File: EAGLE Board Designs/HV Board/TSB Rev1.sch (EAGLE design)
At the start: 148 parts, among them J1 CONNECTOR-4_MOLEX_MICROFIT_PT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, J2 CONNECTOR-3_MOLEX_MICROFIT_PT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, J3 CONNECTOR-8_MF_T_V_, J4 CONNECTOR-3_MOLEX_MICROFIT_PT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, J5 CONNECTOR-4__, K4 RELAY_SPST_NC_POLARIZED_3550_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, K5 RELAY_SPST_NO_3550_12, Q2 TRANSISTOR_N_MOS__PMV15ENEA, U1 LTC6994_1, U10 DCM4623TD2J13D0T70, U11 RELAY_SOLIDSTATE_NC, U15 LOGICGATE_INVERTER_DCKR, U16 LTC3639, U17 VOLTAGE_REGULATOR_ADJ_LR8_SOT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, U18 ISO224B_AIRGAP, U19 ISO224B_AIRGAP, U2 VOLTAGE_REGULATOR_SOT223_5V

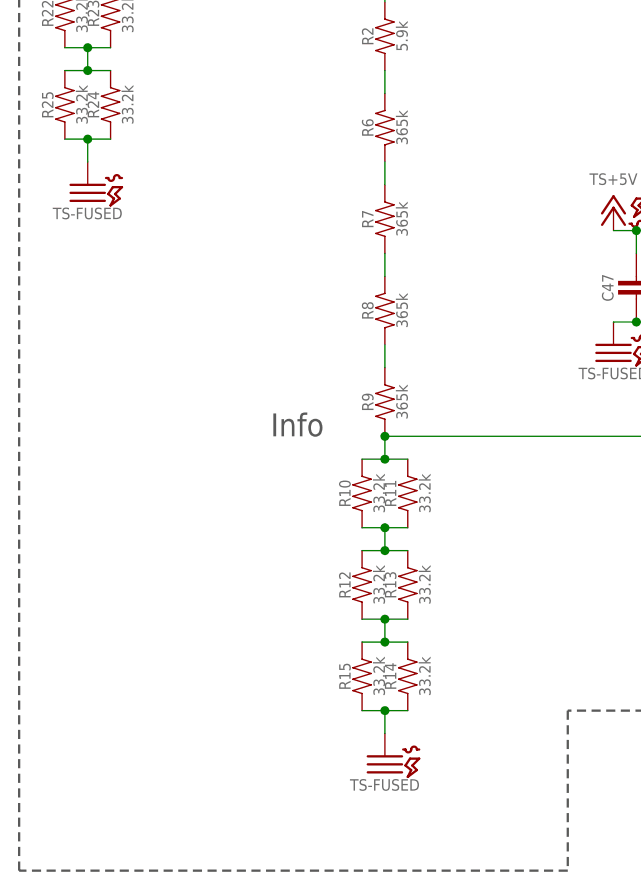
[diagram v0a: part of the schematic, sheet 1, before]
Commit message: fized more erc errors
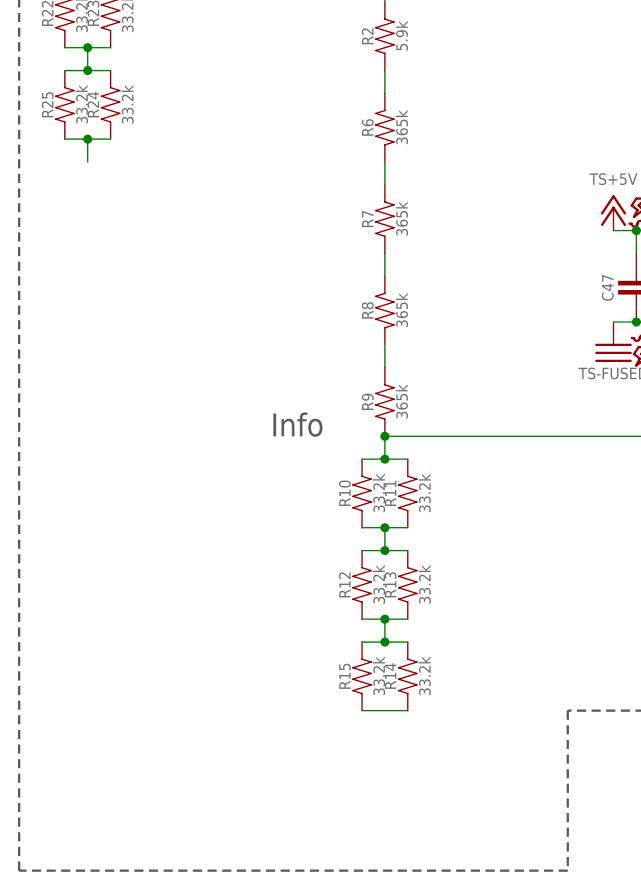
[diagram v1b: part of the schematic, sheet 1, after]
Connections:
- new net N$1: R24.1, R25.1
- new net N$36: R14.1, R15.1
- net TS-FUSED: no longer R14.1, R15.1, R24.1, R25.1
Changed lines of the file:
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@@
 <part name="J4" library="HyTechDevices" deviceset="CONNECTOR-3_?" device="MOLEX_MICROFIT_PTH_VERTICAL_7_DUAL_SPACED2"/>
 <part name="F2" library="HyTechDevices" deviceset="FUSE_?_*" device="0885" technology="1.25"/>
-<part name="U$4" library="HyTechSupplies" deviceset="TS-FUSED" device=""/>
-<part name="U$16" library="HyTechSupplies" deviceset="TS-FUSED" device=""/>
 <part name="U$17" library="HyTechSupplies" deviceset="TS-FUSED" device=""/>
 <part name="U$22" library="HyTechSupplies" deviceset="TS-FUSED" device=""/>
@@
 <attribute name="NAME" x="255.524" y="179.07" size="1.27" layer="96" rot="MR270" align="bottom-center"/>
 </instance>
-<instance part="U$4" gate="G$1" x="17.78" y="93.98" smashed="yes">
-<attribute name="VALUE" x="17.78" y="91.44" size="1.27" layer="96" align="top-center"/>
-</instance>
-<instance part="U$16" gate="G$1" x="50.8" y="30.48" smashed="yes">
-<attribute name="VALUE" x="50.8" y="27.94" size="1.27" layer="96" align="top-center"/>
-</instance>
 <instance part="U$17" gate="G$1" x="96.52" y="50.8" smashed="yes">
 <attribute name="VALUE" x="96.52" y="48.26" size="1.27" layer="96" align="top-center"/>
@@
 </net>
 <net name="TS-FUSED" class="0">
-<segment>
-<pinref part="R25" gate="G$1" pin="1"/>
-<pinref part="R24" gate="G$1" pin="1"/>
-<wire x1="15.24" y1="99.06" x2="17.78" y2="99.06" width="0.1524" layer="91"/>
-<wire x1="17.78" y1="99.06" x2="20.32" y2="99.06" width="0.1524" layer="91"/>
-<wire x1="17.78" y1="99.06" x2="17.78" y2="96.52" width="0.1524" layer="91"/>
-<junction x="17.78" y="99.06"/>
-<pinref part="U$4" gate="G$1" pin="TS-UNFUSED"/>
-</segment>
-<segment>
-<pinref part="R15" gate="G$1" pin="1"/>
-<pinref part="R14" gate="G$1" pin="1"/>
-<wire x1="48.26" y1="35.56" x2="50.8" y2="35.56" width="0.1524" layer="91"/>
-<wire x1="50.8" y1="35.56" x2="53.34" y2="35.56" width="0.1524" layer="91"/>
-<wire x1="50.8" y1="35.56" x2="50.8" y2="33.02" width="0.1524" layer="91"/>
-<junction x="50.8" y="35.56"/>
-<pinref part="U$16" gate="G$1" pin="TS-UNFUSED"/>
-</segment>
 <segment>
 <pinref part="C49" gate="G$1" pin="2"/>
@@
 </segment>
 </net>
+<net name="N$1" class="0">
+<segment>
+<pinref part="R25" gate="G$1" pin="1"/>
+<pinref part="R24" gate="G$1" pin="1"/>
+<wire x1="15.24" y1="99.06" x2="17.78" y2="99.06" width="0.1524" layer="91"/>
+<wire x1="17.78" y1="99.06" x2="20.32" y2="99.06" width="0.1524" layer="91"/>
+<wire x1="17.78" y1="99.06" x2="17.78" y2="96.52" width="0.1524" layer="91"/>
+<junction x="17.78" y="99.06"/>
+</segment>
+</net>
+<net name="N$36" class="0">
+<segment>
+<pinref part="R15" gate="G$1" pin="1"/>
+<pinref part="R14" gate="G$1" pin="1"/>
+<wire x1="48.26" y1="35.56" x2="53.34" y2="35.56" width="0.1524" layer="91"/>
+</segment>
+</net>

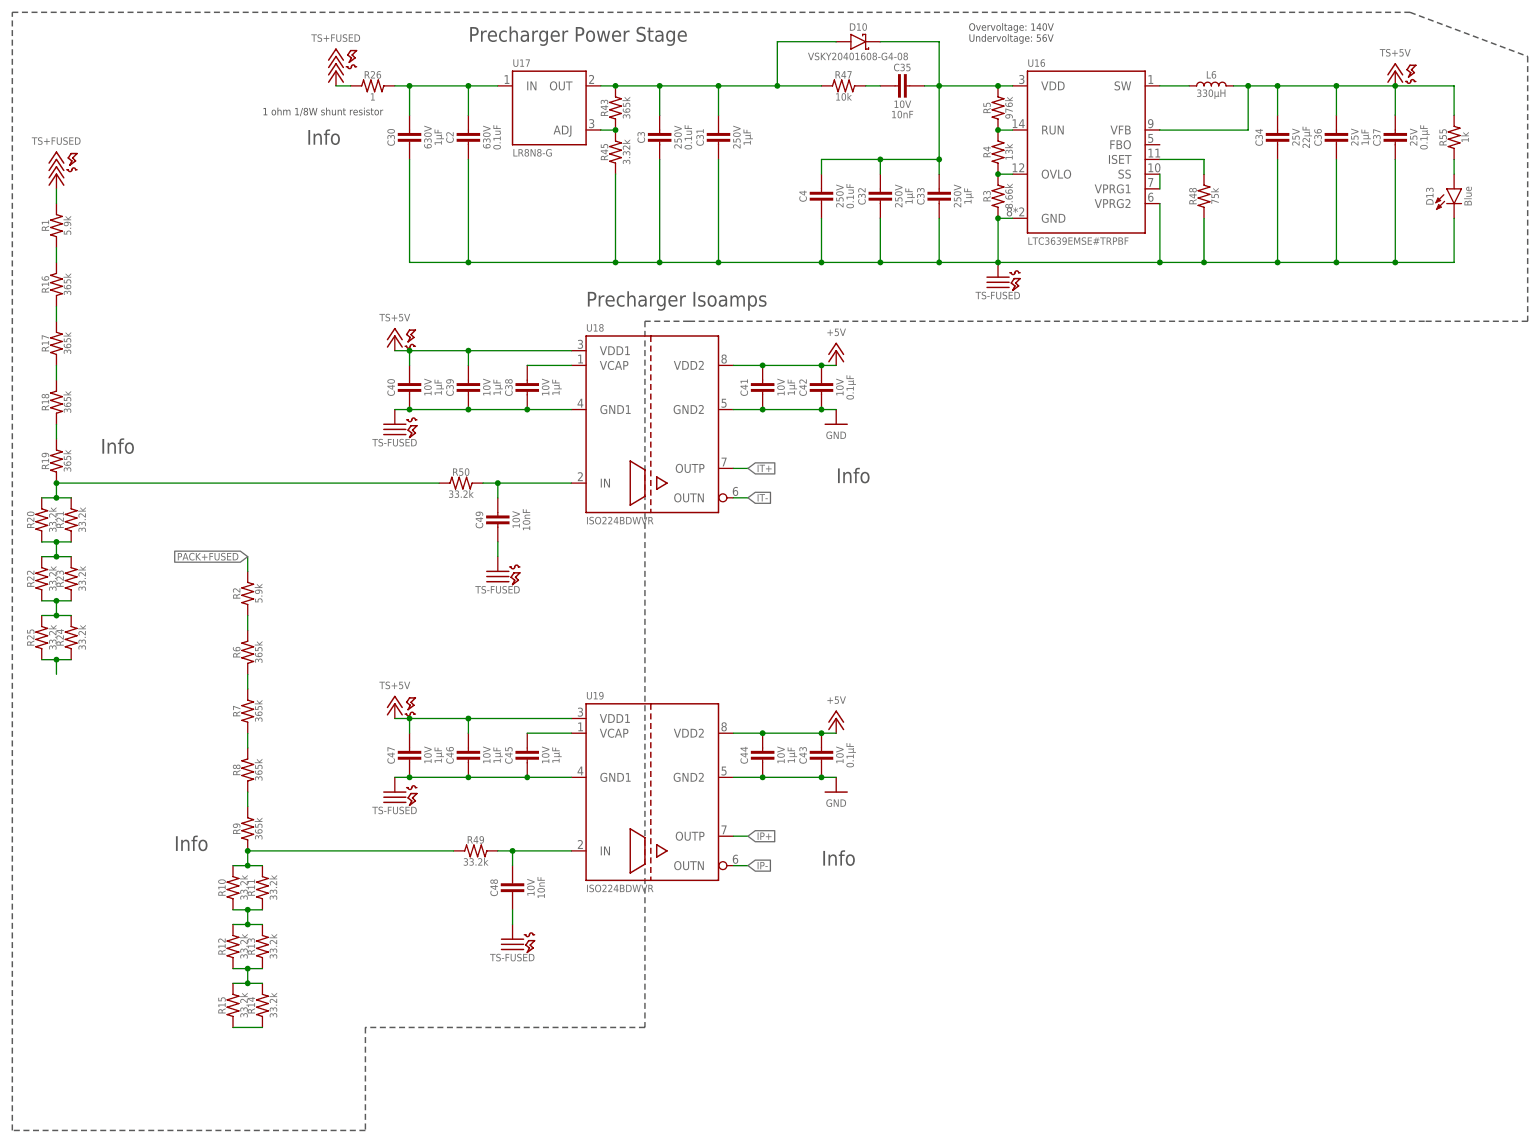
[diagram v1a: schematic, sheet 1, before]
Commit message: Fixed all erc errors
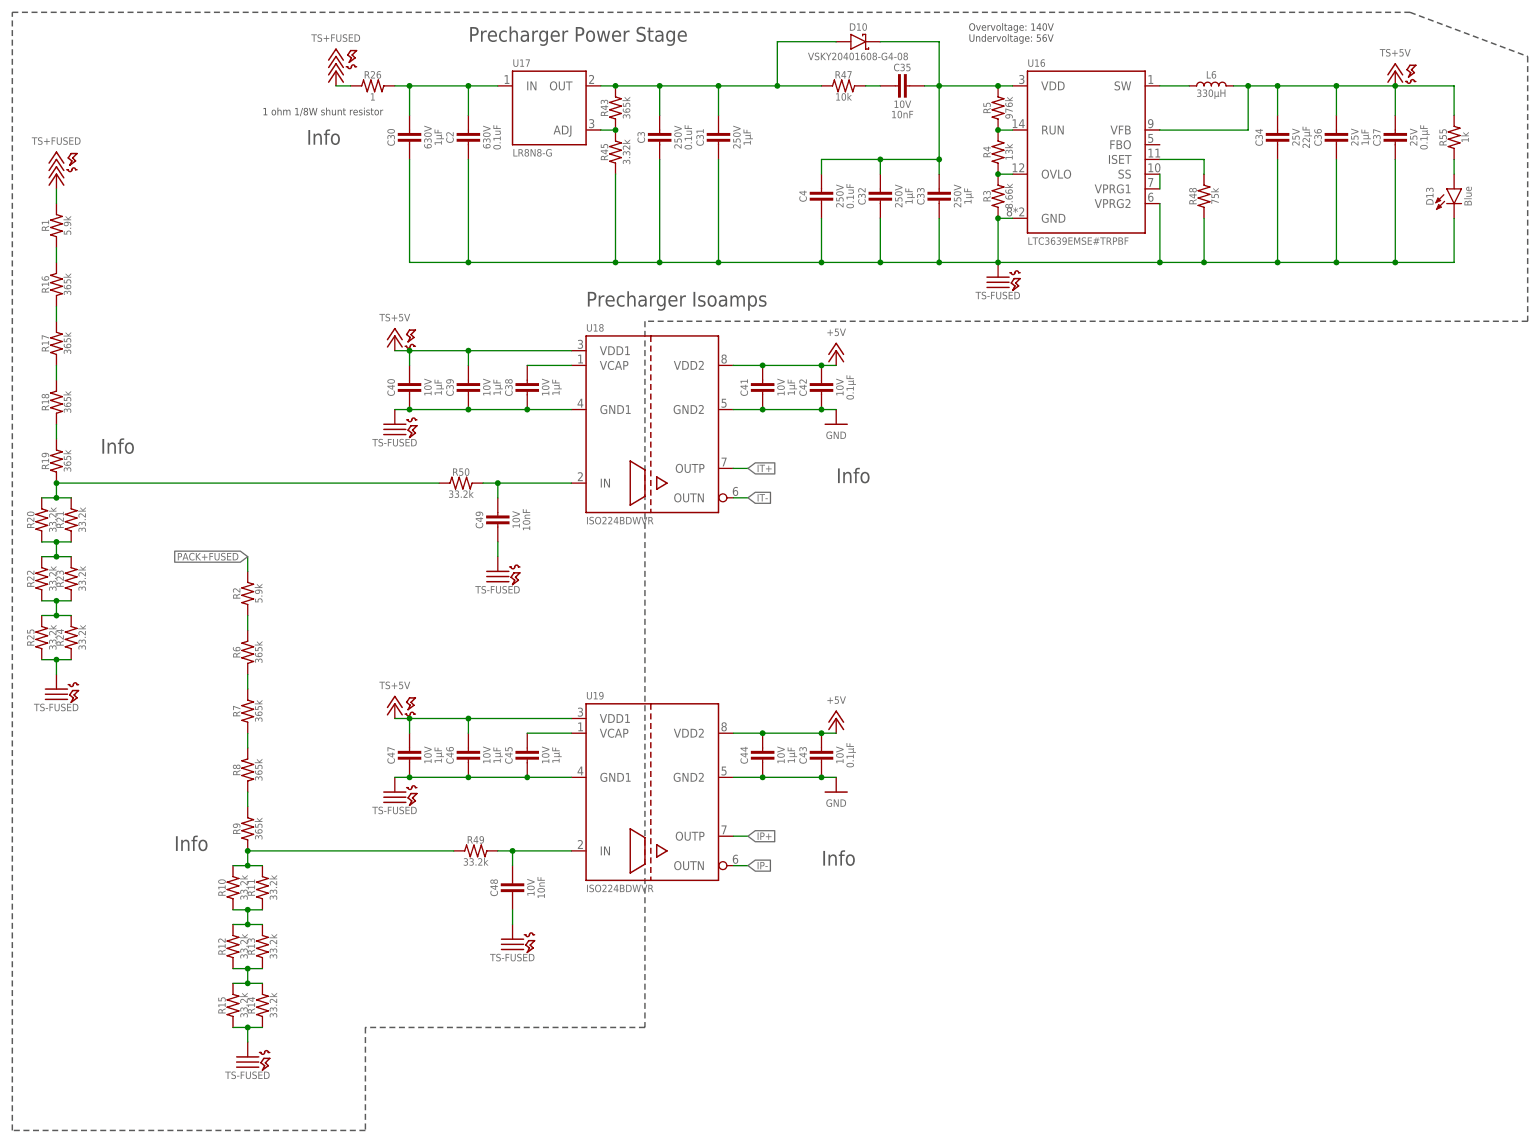
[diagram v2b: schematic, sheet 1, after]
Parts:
- added D14: LED_0603_ORANGE, HyTechDevices:LED_0603_ORANGE
- added R56: RESISTOR_0603_1K, HyTechDevices:RESISTOR_0603_1K
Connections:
- removed net N$36: R14.1, R15.1
- net ENABLE: now also R56.2
- net N$1: now also D14.A, R56.1; no longer R24.1, R25.1
- net TS-FUSED: now also D14.C, F2.2, J1.4, J4.2, R14.1, R15.1, R24.1, R25.1
- net TS-UNFUSED: no longer F2.2, J1.4, J4.2
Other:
- note removed: "LED"
- note removed: "Wrong connector"
- note removed: "fix footprint"

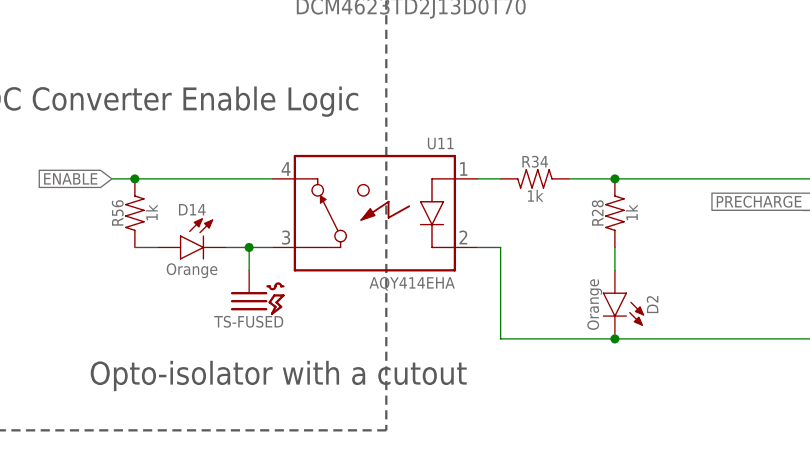
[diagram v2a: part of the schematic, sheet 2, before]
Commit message: Moved connectors around
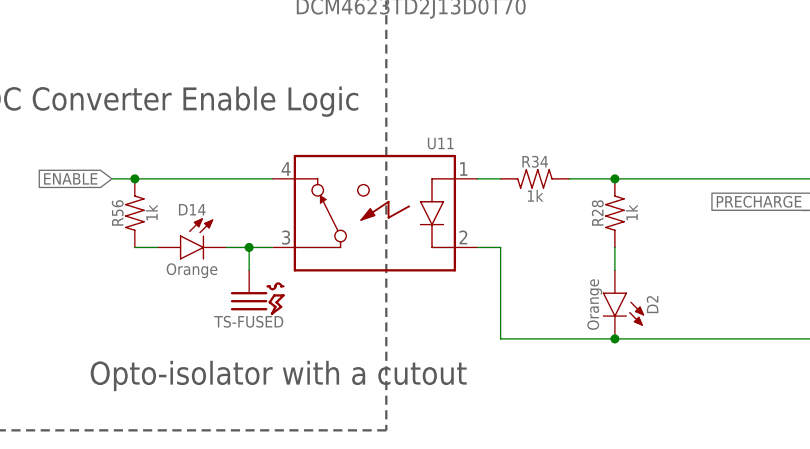
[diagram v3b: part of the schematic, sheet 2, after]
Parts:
- U$1: value RELAY_SOLIDSTATE_NO -> RELAY_SOLIDSTATE_NO_AG; device HyTechDevices:RELAY_SOLIDSTATE_NO -> HyTechDevices:RELAY_SOLIDSTATE_NO_AG
- U11: value RELAY_SOLIDSTATE_NC -> RELAY_SOLIDSTATE_NC_AG; device HyTechDevices:RELAY_SOLIDSTATE_NC -> HyTechDevices:RELAY_SOLIDSTATE_NC_AG

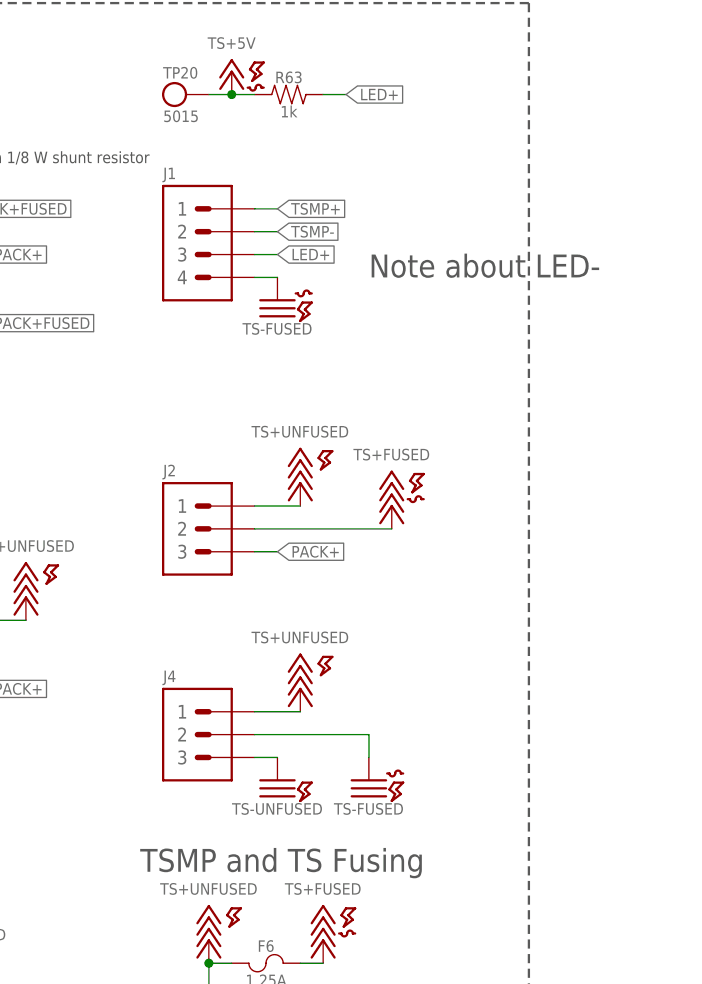
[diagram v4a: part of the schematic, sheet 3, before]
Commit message: Moved parts to be grouped together in their respective parts
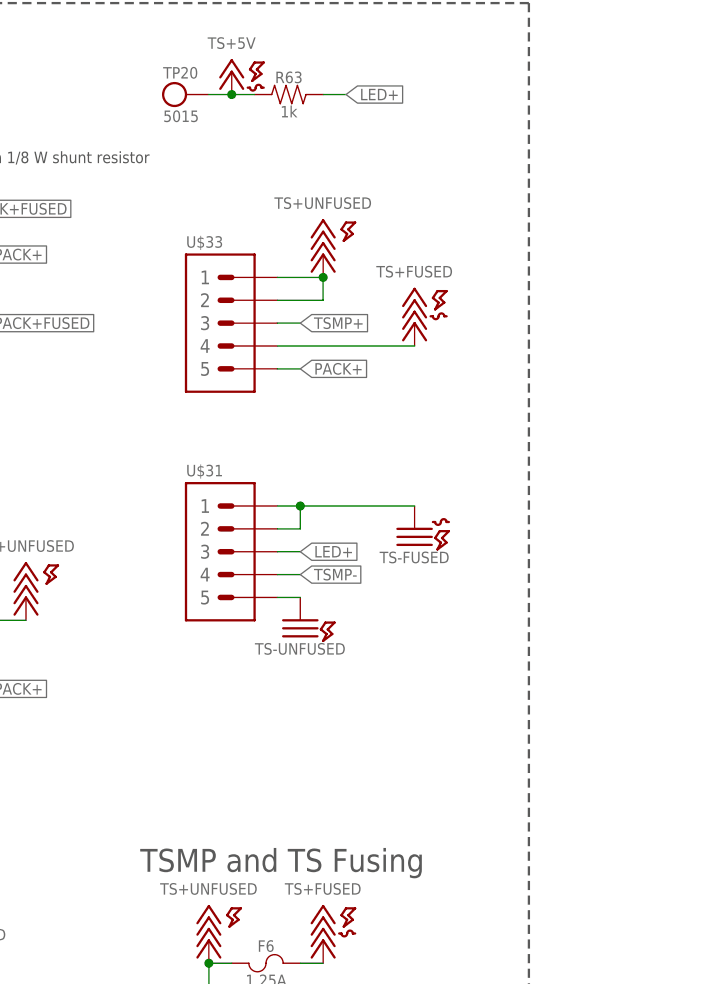
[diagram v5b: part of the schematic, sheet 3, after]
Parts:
- removed J1: CONNECTOR-4_MOLEX_MICROFIT_PTH_VERTICAL_07_DUAL_SPACED_, HyTechDevices:CONNECTOR-4_MOLEX_MICROFIT_PTH_VERTICAL_07_DUAL_SPACED_
- removed J2: CONNECTOR-3_MOLEX_MICROFIT_PTH_VERTICAL_5_DUAL_SPACED, HyTechDevices:CONNECTOR-3_MOLEX_MICROFIT_PTH_VERTICAL_5_DUAL_SPACED
- removed J4: CONNECTOR-3_MOLEX_MICROFIT_PTH_VERTICAL_7_DUAL_SPACED2, HyTechDevices:CONNECTOR-3_MOLEX_MICROFIT_PTH_VERTICAL_7_DUAL_SPACED2
- added U$31: CONNECTOR-5_6_SPACED_, HyTechDevices:CONNECTOR-5_6_SPACED_
- added U$33: CONNECTOR-5_7_SPACED_, HyTechDevices:CONNECTOR-5_7_SPACED_
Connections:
- net LED+: now also U$31.3; no longer J1.3
- net PACK+: now also U$33.5; no longer J2.3
- net TS+FUSED: now also U$33.4; no longer J2.2
- net TS+UNFUSED: now also U$33.1, U$33.2; no longer J2.1, J4.1
- net TS-FUSED: now also U$31.1, U$31.2; no longer J1.4, J4.2
- net TS-UNFUSED: now also U$31.5; no longer J4.3
- net TSMP+: now also U$33.3; no longer J1.1
- net TSMP-: now also U$31.4; no longer J1.2
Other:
- note removed: "Note about LED-"

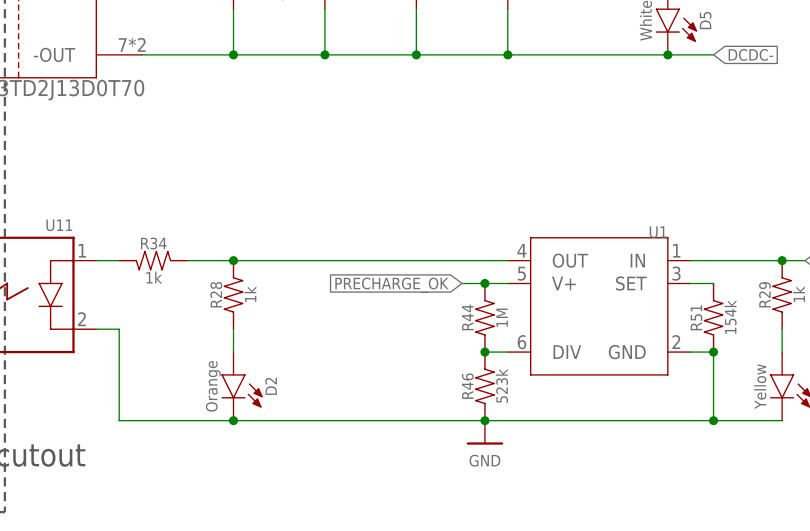
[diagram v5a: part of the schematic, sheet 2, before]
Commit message: Board layout and tracing underway
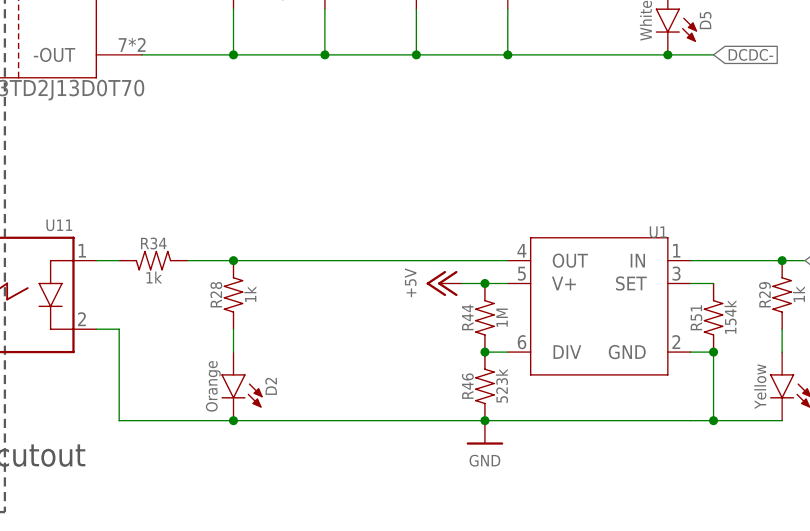
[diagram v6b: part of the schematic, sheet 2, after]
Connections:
- net +5V: now also R44.2, U1.V+
- net PRECHARGE_OK: no longer R44.2, U1.V+
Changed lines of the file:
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@@
 <part name="U$31" library="HyTechDevices" deviceset="CONNECTOR-5_?_*" device="6_SPACED"/>
 <part name="U$33" library="HyTechDevices" deviceset="CONNECTOR-5_?_*" device="7_SPACED"/>
+<part name="P18" library="HyTechSupplies" deviceset="+5V" device=""/>
 </parts>
 <sheets>
@@
 <attribute name="NAME" x="115.57" y="120.396" size="1.27" layer="96" align="bottom-center"/>
 </instance>
+<instance part="P18" gate="1" x="185.42" y="121.92" smashed="yes" rot="R90">
+<attribute name="VALUE" x="182.88" y="121.92" size="1.27" layer="96" rot="R90" align="bottom-center"/>
+</instance>
 </instances>
 <busses>
@@
 </net>
 <net name="PRECHARGE_OK" class="0">
-<segment>
-<pinref part="R44" gate="G$1" pin="2"/>
-<pinref part="U1" gate="G$1" pin="V+"/>
-<wire x1="190.5" y1="121.92" x2="193.04" y2="121.92" width="0.1524" layer="91"/>
-<wire x1="190.5" y1="121.92" x2="187.96" y2="121.92" width="0.1524" layer="91"/>
-<junction x="190.5" y="121.92"/>
-<label x="187.96" y="121.92" size="1.27" layer="95" rot="R180" xref="yes"/>
-</segment>
 <segment>
 <pinref part="U1" gate="G$1" pin="IN"/>
@@
 </segment>
 </net>
+<net name="+5V" class="0">
+<segment>
+<pinref part="U1" gate="G$1" pin="V+"/>
+<pinref part="R44" gate="G$1" pin="2"/>
+<wire x1="193.04" y1="121.92" x2="190.5" y2="121.92" width="0.1524" layer="91"/>
+<wire x1="190.5" y1="121.92" x2="187.96" y2="121.92" width="0.1524" layer="91"/>
+<junction x="190.5" y="121.92"/>
+<pinref part="P18" gate="1" pin="+5V"/>
+</segment>
+</net>
